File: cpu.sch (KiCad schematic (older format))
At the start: 24 parts, among them P24 CONN_3X2, P25 Load, U1 MC9S12XDP512, X1 16MHz

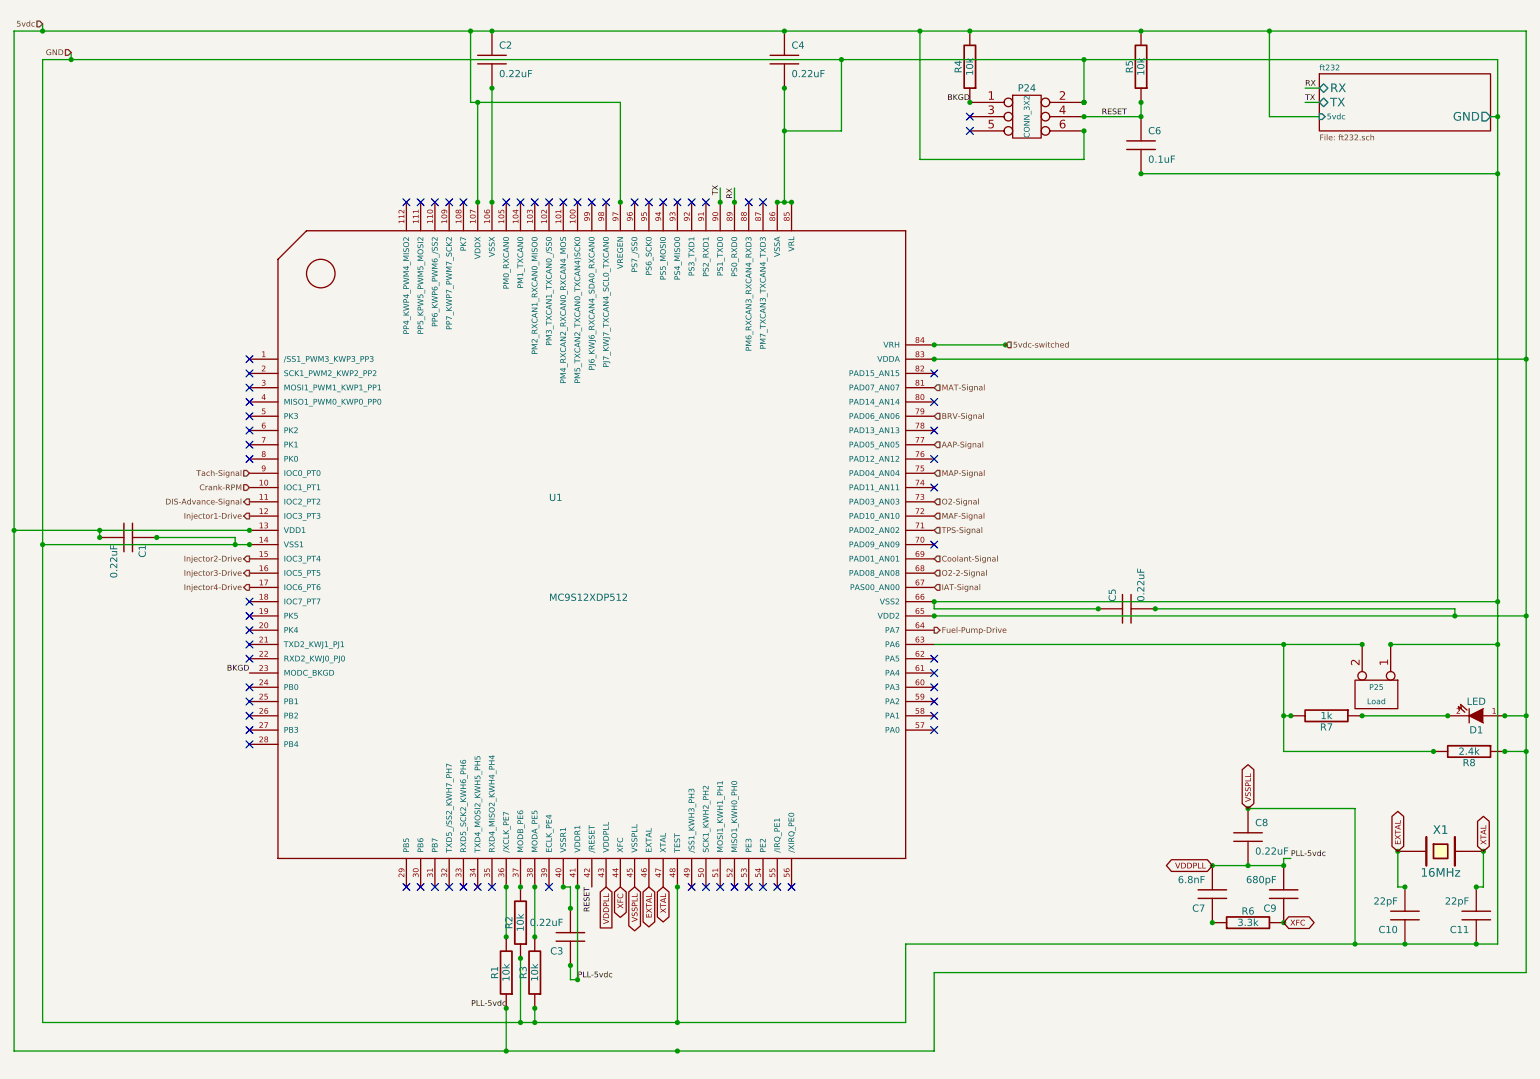
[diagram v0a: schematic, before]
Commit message: Redesigned schematics and board
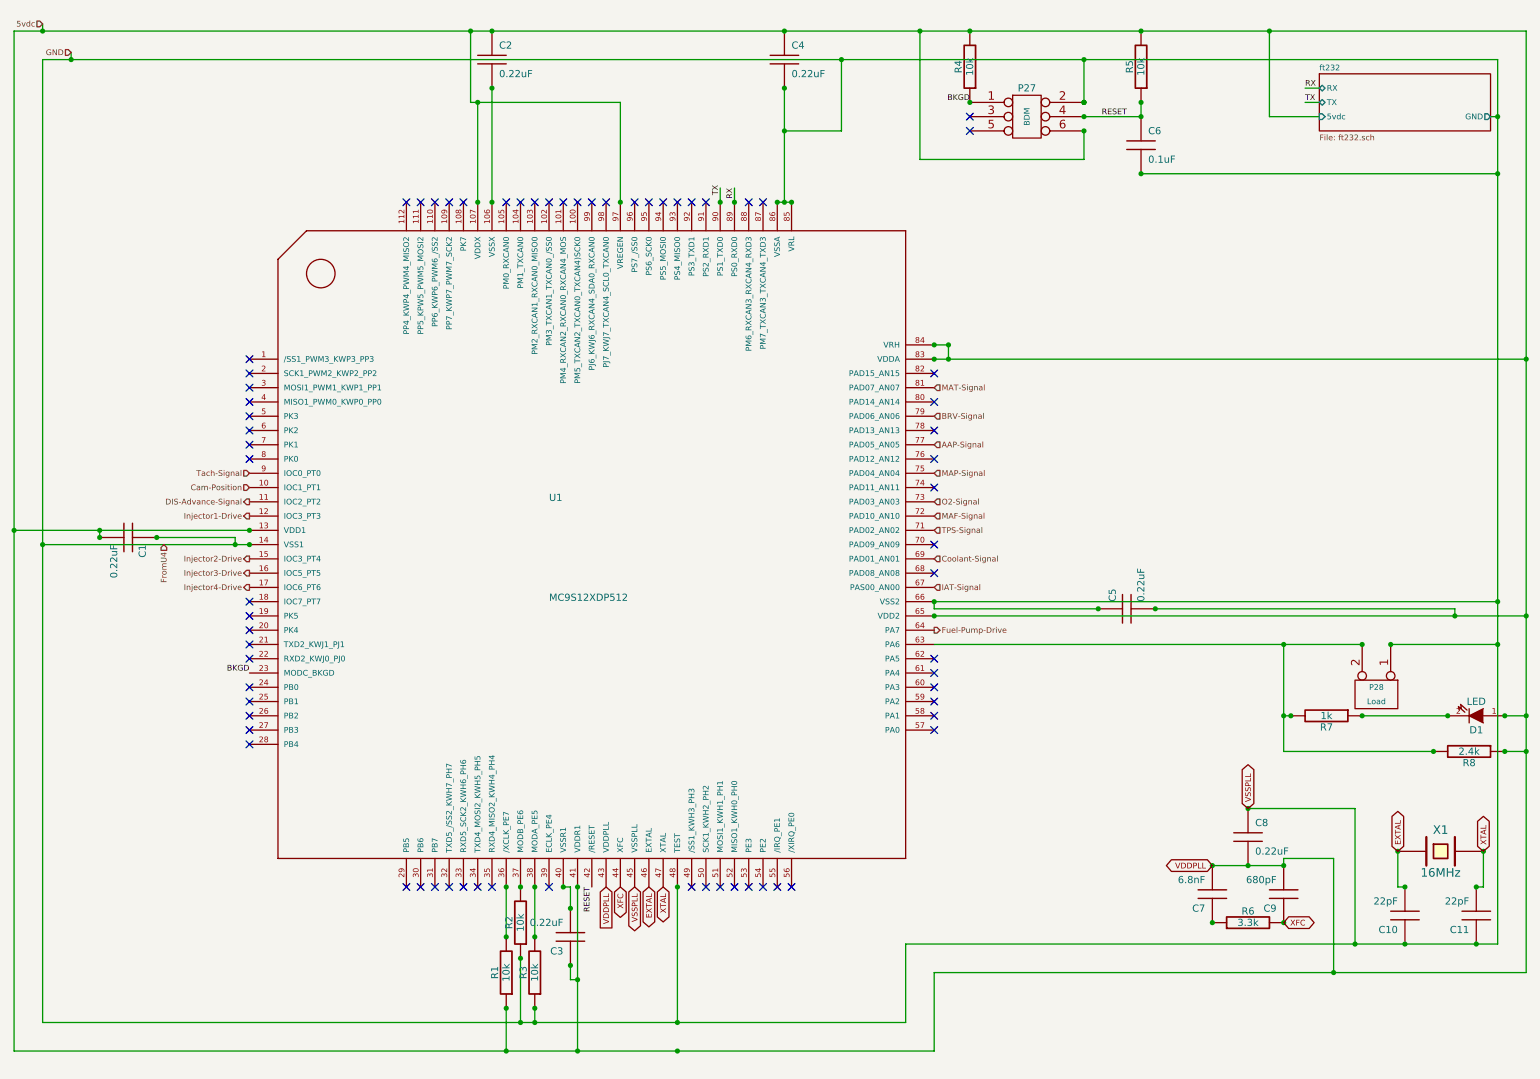
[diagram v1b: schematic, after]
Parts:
- P27: renamed from P24; value CONN_3X2 -> BDM
- renumbered P25 to P28
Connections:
- net 5vdc-switched is gone; now on net VDDPLL: U1.84 (VRH)
- net Crank-RPM renamed Cam-Position
- net O2-2-Signal: no longer names the net of U1.68 (PAD08_AN08)
- no-connect marks 69 -> 70

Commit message: Updated Schematics, created new PDF, completed board layout and routing
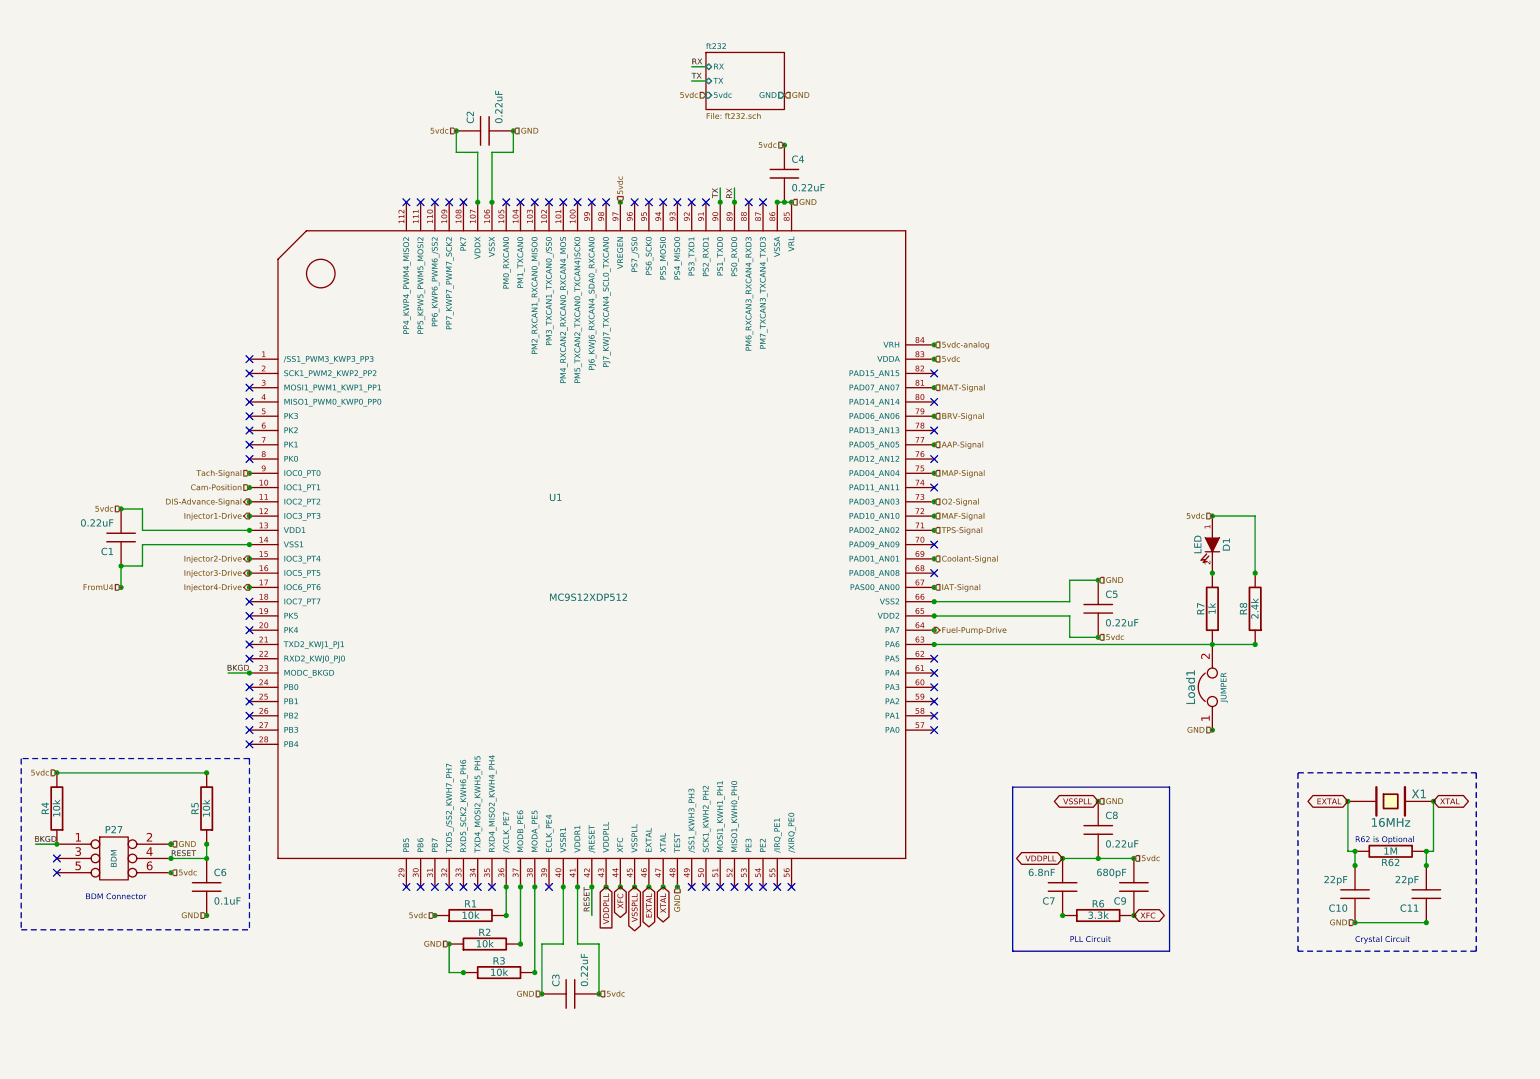
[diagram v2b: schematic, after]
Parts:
- removed P28: Load, symbol CONN_2
- added Load1: JUMPER, symbol JUMPER
- added R62: 1M, symbol R
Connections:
- net labels added: 5vdc-analog
- wire segments 80 -> 52
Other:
- note added: "BDM Connector"
- note added: "Crystal Circuit"
- note added: "PLL Circuit"
- note added: "R62 is Optional"
- moved on the sheet: C1, C10, C11, C2, C3, C4, C5, C6, C7, C8, C9, D1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

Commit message: Modified: schematics to correct errors
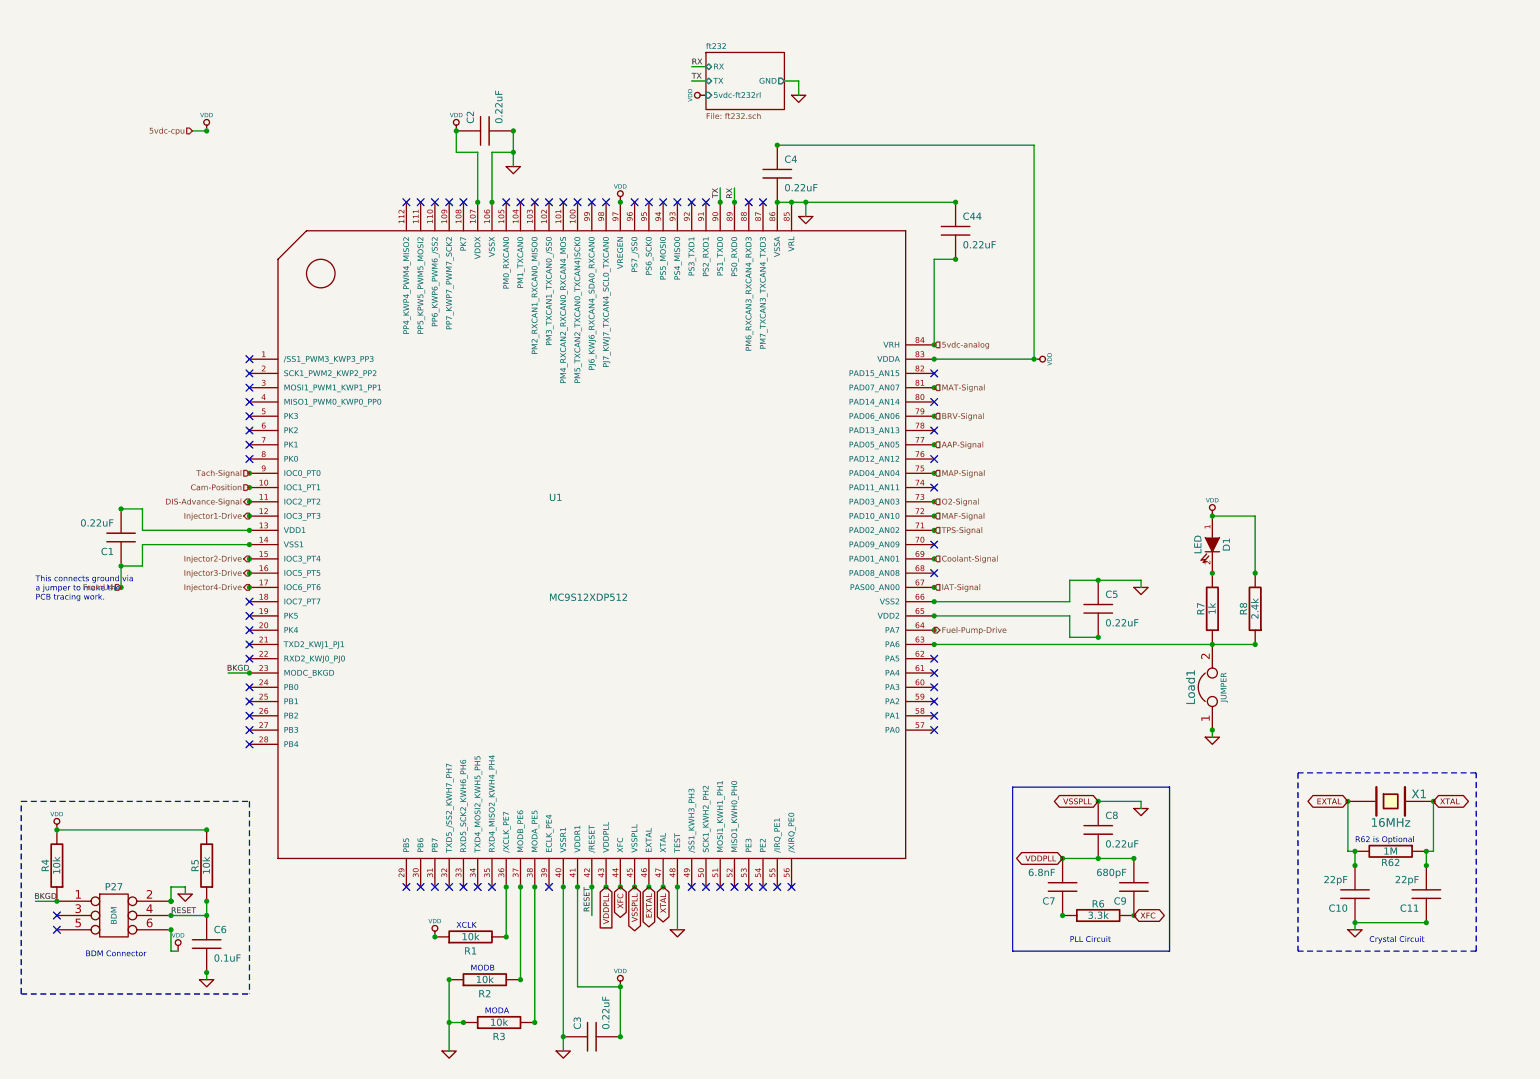
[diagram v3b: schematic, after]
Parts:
- added C44: 0.22uF, symbol C
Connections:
- net labels added: 5vdc-cpu, VDD
- net labels removed: 5vdc
- wire segments 52 -> 71
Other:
- note added: "MODA"
- note added: "MODB"
- note added: "This connects ground via \na jumper to make the \nPCB tracing work."
- note added: "XCLK"
- moved on the sheet: C3, C4, C6, P27, R1, R2, R3, R4, R5

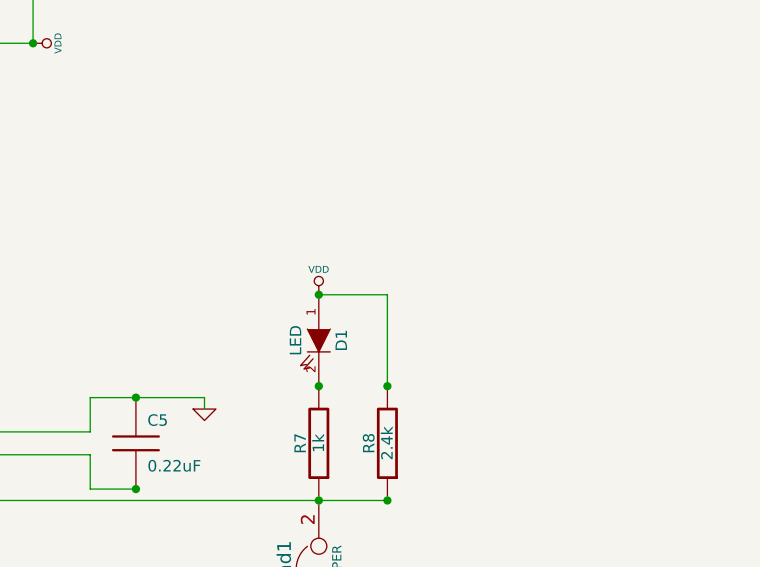
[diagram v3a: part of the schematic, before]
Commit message: Improved schematic, re-design board, re-created PDF
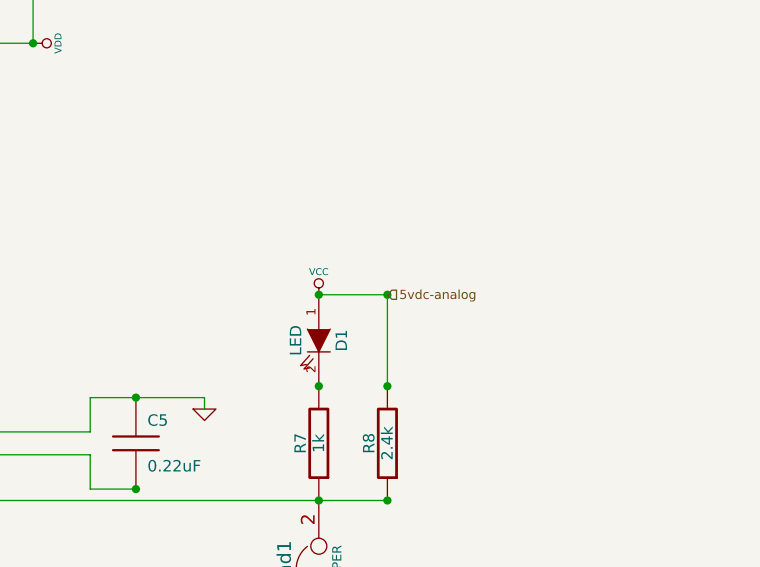
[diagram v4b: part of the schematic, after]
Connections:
- net labels added: VCC
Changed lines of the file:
@@
-EESchema Schematic File Version 2  date Sun 22 Jan 2012 05:59:51 PM EST
+EESchema Schematic File Version 2  date Mon 23 Jan 2012 07:28:42 AM EST
 LIBS:power
 LIBS:device
@@
 $Descr A4 11700 8267
 Sheet 6 7
-Title ""
-Date "22 jan 2012"
-Rev ""
-Comp ""
+Title "Jaguar PCB for FreeEMS"
+Date "23 jan 2012"
+Rev "A.1"
+Comp "diyefi.org"
 Comment1 ""
 Comment2 ""
@@
 Comment4 ""
 $EndDescr
+Text HLabel 9250 3950 2    40   Input ~ 0
+5vdc-analog
+Connection ~ 9250 3950
+$Comp
+L VCC #PWR033
+U 1 1 4F1CE2A5
+P 8950 3950
+F 0 "#PWR033" H 8950 4050 30  0001 C CNN
+F 1 "VCC" H 8950 4050 30  0000 C CNN
+	1    8950 3950
+	1    0    0    -1
+$EndComp
 Connection ~ 7150 2150
 Connection ~ 5900 1350
@@
 $EndComp
 $Comp
-L VDD #PWR14
+L VDD #PWR034
 U 1 1 4F1C3492
 P 5400 1000
-F 0 "#PWR14" H 5400 1100 30  0001 C CNN
+F 0 "#PWR034" H 5400 1100 30  0001 C CNN
 F 1 "VDD" H 5400 1110 30  0000 C CNN
 	1    5400 1000
@@
 $EndComp
 $Comp
-L VDD #PWR2
+L VDD #PWR035
 U 1 1 4F1C343C
 P 1700 7000
-F 0 "#PWR2" H 1700 7100 30  0001 C CNN
+F 0 "#PWR035" H 1700 7100 30  0001 C CNN
 F 1 "VDD" H 1700 7110 30  0000 C CNN
 	1    1700 7000
@@
 $EndComp
 $Comp
-L VDD #PWR1
+L VDD #PWR036
 U 1 1 4F1C31B7
 P 850 6150
-F 0 "#PWR1" H 850 6250 30  0001 C CNN
+F 0 "#PWR036" H 850 6250 30  0001 C CNN
 F 1 "VDD" H 850 6260 30  0000 C CNN
 	1    850  6150
@@
 $EndComp
 $Comp
-L VDD #PWR6
+L VDD #PWR037
 U 1 1 4F1C31AA
 P 3500 6900
-F 0 "#PWR6" H 3500 7000 30  0001 C CNN
+F 0 "#PWR037" H 3500 7000 30  0001 C CNN
 F 1 "VDD" H 3500 7010 30  0000 C CNN
 	1    3500 6900
@@
 $EndComp
 $Comp
-L VDD #PWR12
+L VDD #PWR038
 U 1 1 4F1C3179
 P 4800 7250
-F 0 "#PWR12" H 4800 7350 30  0001 C CNN
+F 0 "#PWR038" H 4800 7350 30  0001 C CNN
 F 1 "VDD" H 4800 7360 30  0000 C CNN
 	1    4800 7250
@@
 $EndComp
 $Comp
-L GND #PWR13
+L GND #PWR039
 U 1 1 4F1C316A
 P 5200 6850
-F 0 "#PWR13" H 5200 6850 30  0001 C CNN
+F 0 "#PWR039" H 5200 6850 30  0001 C CNN
 F 1 "GND" H 5200 6780 30  0001 C CNN
 	1    5200 6850
@@
 $EndComp
 $Comp
-L GND #PWR19
+L GND #PWR040
 U 1 1 4F1C3153
 P 8450 6000
-F 0 "#PWR19" H 8450 6000 30  0001 C CNN
+F 0 "#PWR040" H 8450 6000 30  0001 C CNN
 F 1 "GND" H 8450 5930 30  0001 C CNN
 	1    8450 6000
@@
 $EndComp
 $Comp
-L VDD #PWR20
-U 1 1 4F1C3140
-P 8950 3950
-F 0 "#PWR20" H 8950 4050 30  0001 C CNN
-F 1 "VDD" H 8950 4060 30  0000 C CNN
-	1    8950 3950
-	1    0    0    -1
-$EndComp
-$Comp
-L VDD #PWR17
+L VDD #PWR041
 U 1 1 4F1C3124
 P 7700 2850
-F 0 "#PWR17" H 7700 2950 30  0001 C CNN
+F 0 "#PWR041" H 7700 2950 30  0001 C CNN
 F 1 "VDD" H 7700 2960 30  0000 C CNN
 	1    7700 2850
@@
 $EndComp
 $Comp
-L VDD #PWR11
+L VDD #PWR042
 U 1 1 4F1C3115
 P 4800 1750
-F 0 "#PWR11" H 4800 1850 30  0001 C CNN
+F 0 "#PWR042" H 4800 1850 30  0001 C CNN
 F 1 "VDD" H 4800 1860 30  0000 C CNN
 	1    4800 1750
@@
 $EndComp
 $Comp
-L VDD #PWR4
+L VDD #PWR043
 U 1 1 4F1C30FA
 P 1900 1250
-F 0 "#PWR4" H 1900 1350 30  0001 C CNN
+F 0 "#PWR043" H 1900 1350 30  0001 C CNN
 F 1 "VDD" H 1900 1360 30  0000 C CNN
 	1    1900 1250
@@
 $EndComp
 $Comp
-L VDD #PWR8
+L VDD #PWR044
 U 1 1 4F1C30DD
 P 3650 1250
-F 0 "#PWR8" H 3650 1350 30  0001 C CNN
+F 0 "#PWR044" H 3650 1350 30  0001 C CNN
 F 1 "VDD" H 3650 1360 30  0000 C CNN
 	1    3650 1250
@@
 $EndComp
 $Comp
-L GND #PWR3
+L GND #PWR045
 U 1 1 4F1C290C
 P 1750 6600
-F 0 "#PWR3" H 1750 6600 30  0001 C CNN
+F 0 "#PWR045" H 1750 6600 30  0001 C CNN
 F 1 "GND" H 1750 6530 30  0001 C CNN
 	1    1750 6600
@@
 $EndComp
 $Comp
-L GND #PWR5
+L GND #PWR046
 U 1 1 4F1C2905
 P 1900 7200
-F 0 "#PWR5" H 1900 7200 30  0001 C CNN
+F 0 "#PWR046" H 1900 7200 30  0001 C CNN
 F 1 "GND" H 1900 7130 30  0001 C CNN
 	1    1900 7200
@@
 This connects ground via \na jumper to make the \nPCB tracing work.
 $Comp
-L GND #PWR9
+L GND #PWR047
 U 1 1 4F1C289E
 P 4050 1500
-F 0 "#PWR9" H 4050 1500 30  0001 C CNN
+F 0 "#PWR047" H 4050 1500 30  0001 C CNN
 F 1 "GND" H 4050 1430 30  0001 C CNN
 	1    4050 1500
@@
 $EndComp
 $Comp
-L GND #PWR15
+L GND #PWR048
 U 1 1 4F1C287C
 P 6050 1000
-F 0 "#PWR15" H 6050 1000 30  0001 C CNN
+F 0 "#PWR048" H 6050 1000 30  0001 C CNN
 F 1 "GND" H 6050 930 30  0001 C CNN
 	1    6050 1000
@@
 $EndComp
 $Comp
-L GND #PWR16
+L GND #PWR049
 U 1 1 4F1C2863
 P 6100 1850
-F 0 "#PWR16" H 6100 1850 30  0001 C CNN
+F 0 "#PWR049" H 6100 1850 30  0001 C CNN
 F 1 "GND" H 6100 1780 30  0001 C CNN
 	1    6100 1850
@@
 $EndComp
 $Comp
-L GND #PWR21
+L GND #PWR050
 U 1 1 4F1C284A
 P 8950 5500
-F 0 "#PWR21" H 8950 5500 30  0001 C CNN
+F 0 "#PWR050" H 8950 5500 30  0001 C CNN
 F 1 "GND" H 8950 5430 30  0001 C CNN
 	1    8950 5500
@@
 $EndComp
 $Comp
-L GND #PWR18
+L GND #PWR051
 U 1 1 4F1C2831
 P 8450 4450
-F 0 "#PWR18" H 8450 4450 30  0001 C CNN
+F 0 "#PWR051" H 8450 4450 30  0001 C CNN
 F 1 "GND" H 8450 4380 30  0001 C CNN
 	1    8450 4450
@@
 $EndComp
 $Comp
-L GND #PWR22
+L GND #PWR052
 U 1 1 4F1C2808
 P 9950 6850
-F 0 "#PWR22" H 9950 6850 30  0001 C CNN
+F 0 "#PWR052" H 9950 6850 30  0001 C CNN
 F 1 "GND" H 9950 6780 30  0001 C CNN
 	1    9950 6850
@@
 XCLK
 $Comp
-L GND #PWR10
+L GND #PWR053
 U 1 1 4F1C2798
 P 4400 7700
-F 0 "#PWR10" H 4400 7700 30  0001 C CNN
+F 0 "#PWR053" H 4400 7700 30  0001 C CNN
 F 1 "GND" H 4400 7630 30  0001 C CNN
 	1    4400 7700
@@
 $EndComp
 $Comp
-L GND #PWR7
+L GND #PWR054
 U 1 1 4F1C273A
 P 3600 7700
-F 0 "#PWR7" H 3600 7700 30  0001 C CNN
+F 0 "#PWR054" H 3600 7700 30  0001 C CNN
 F 1 "GND" H 3600 7630 30  0001 C CNN
 	1    3600 7700
